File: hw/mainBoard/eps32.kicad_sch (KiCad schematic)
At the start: 13 parts, among them SW1 SW_Push, SW2 SW_Push, U1 ESP32-WROOM-E, U4 TLV76133DCYR

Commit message: finale bez rybicky
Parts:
- U2: renamed from U4; footprint SOT_8DCYR_TEX -> TLV761:SOT_8DCYR_TEX
- renumbered C6 to C1, C7 to C2, C1 to C4, C2 to C5, C5 to C8, C4 to C9
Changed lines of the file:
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@@
   (symbol (lib_id "Device:C") (at 93.98 116.84 90) (unit 1)
     (in_bom yes) (on_board yes) (dnp no)
-    (property "Reference" "C7" (at 93.98 120.65 90)
+    (property "Reference" "C2" (at 93.98 120.65 90)
       (effects (font (size 1.27 1.27)))
     )
@@
       (project "mainBoard"
         (path "/afbe4b5f-4e5c-4a12-a44b-208d158a3f7a/b91751a5-b1b1-4084-8612-1e1796d0f474"
-          (reference "C7") (unit 1)
+          (reference "C2") (unit 1)
         )
       )
@@
   (symbol (lib_id "Device:C") (at 68.58 38.1 0) (unit 1)
     (in_bom yes) (on_board yes) (dnp no) (fields_autoplaced)
-    (property "Reference" "C4" (at 72.39 36.83 0)
+    (property "Reference" "C9" (at 72.39 36.83 0)
       (effects (font (size 1.27 1.27)) (justify left))
     )
@@
       (project "mainBoard"
         (path "/afbe4b5f-4e5c-4a12-a44b-208d158a3f7a/b91751a5-b1b1-4084-8612-1e1796d0f474"
-          (reference "C4") (unit 1)
+          (reference "C9") (unit 1)
         )
       )
@@
   (symbol (lib_id "Device:C") (at 45.72 116.84 90) (unit 1)
     (in_bom yes) (on_board yes) (dnp no)
-    (property "Reference" "C6" (at 45.72 120.65 90)
+    (property "Reference" "C1" (at 45.72 120.65 90)
       (effects (font (size 1.27 1.27)))
     )
@@
       (project "mainBoard"
         (path "/afbe4b5f-4e5c-4a12-a44b-208d158a3f7a/b91751a5-b1b1-4084-8612-1e1796d0f474"
-          (reference "C6") (unit 1)
+          (reference "C1") (unit 1)
         )
       )
@@
   (symbol (lib_id "Device:C") (at 93.98 81.28 0) (unit 1)
     (in_bom yes) (on_board yes) (dnp no) (fields_autoplaced)
-    (property "Reference" "C2" (at 97.79 80.01 0)
+    (property "Reference" "C5" (at 97.79 80.01 0)
       (effects (font (size 1.27 1.27)) (justify left))
     )
@@
       (project "mainBoard"
         (path "/afbe4b5f-4e5c-4a12-a44b-208d158a3f7a/b91751a5-b1b1-4084-8612-1e1796d0f474"
-          (reference "C2") (unit 1)
+          (reference "C5") (unit 1)
         )
       )
@@
   (symbol (lib_id "TLV761:PTLV76118DCYR") (at 54.61 27.94 0) (unit 1)
     (in_bom yes) (on_board yes) (dnp no)
-    (property "Reference" "U4" (at 85.09 20.32 0)
+    (property "Reference" "U2" (at 85.09 20.32 0)
       (effects (font (size 1.524 1.524)))
     )
@@
       (effects (font (size 1.524 1.524)))
     )
-    (property "Footprint" "SOT_8DCYR_TEX" (at 54.61 27.94 0)
+    (property "Footprint" "TLV761:SOT_8DCYR_TEX" (at 54.61 27.94 0)
       (effects (font (size 1.27 1.27) italic) hide)
     )
@@
       (project "mainBoard"
         (path "/afbe4b5f-4e5c-4a12-a44b-208d158a3f7a/b91751a5-b1b1-4084-8612-1e1796d0f474"
-          (reference "U4") (unit 1)
+          (reference "U2") (unit 1)
         )
       )
@@
   (symbol (lib_id "Device:C") (at 111.76 35.56 0) (unit 1)
     (in_bom yes) (on_board yes) (dnp no) (fields_autoplaced)
-    (property "Reference" "C5" (at 115.57 34.29 0)
+    (property "Reference" "C8" (at 115.57 34.29 0)
       (effects (font (size 1.27 1.27)) (justify left))
     )
@@
       (project "mainBoard"
         (path "/afbe4b5f-4e5c-4a12-a44b-208d158a3f7a/b91751a5-b1b1-4084-8612-1e1796d0f474"
-          (reference "C5") (unit 1)
+          (reference "C8") (unit 1)
         )
       )
@@
   (symbol (lib_id "Device:C") (at 45.72 68.58 0) (unit 1)
     (in_bom yes) (on_board yes) (dnp no) (fields_autoplaced)
-    (property "Reference" "C1" (at 49.53 67.31 0)
+    (property "Reference" "C4" (at 49.53 67.31 0)
       (effects (font (size 1.27 1.27)) (justify left))
     )
@@
       (project "mainBoard"
         (path "/afbe4b5f-4e5c-4a12-a44b-208d158a3f7a/b91751a5-b1b1-4084-8612-1e1796d0f474"
-          (reference "C1") (unit 1)
-        )
-      )
+          (reference "C4") (unit 1)
+        )
+      )

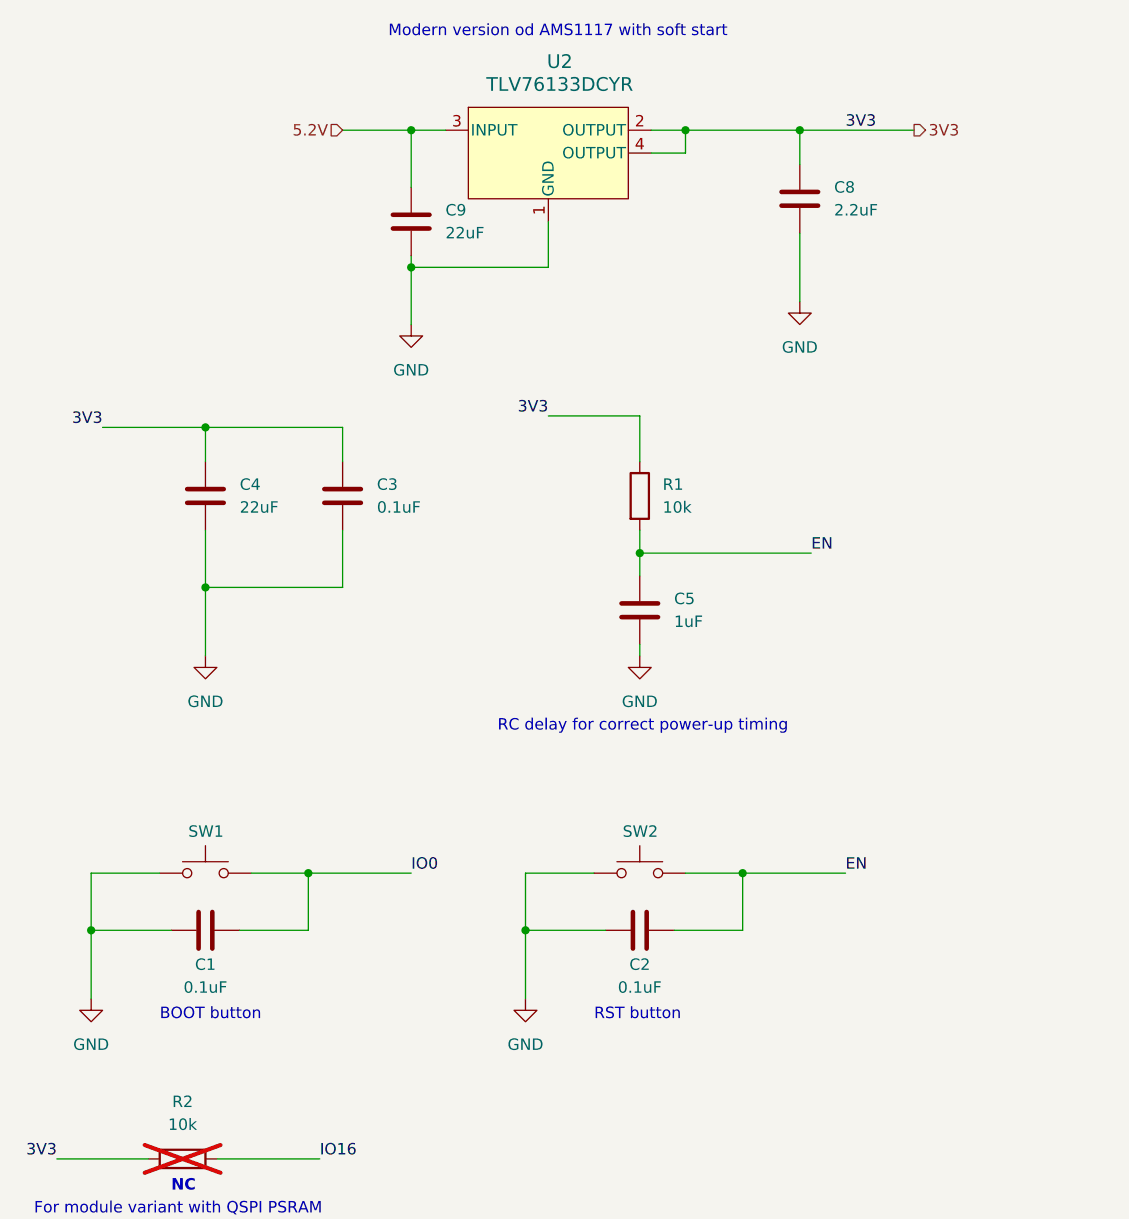
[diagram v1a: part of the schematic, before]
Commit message: text - periferie, obrazky hw - schemata
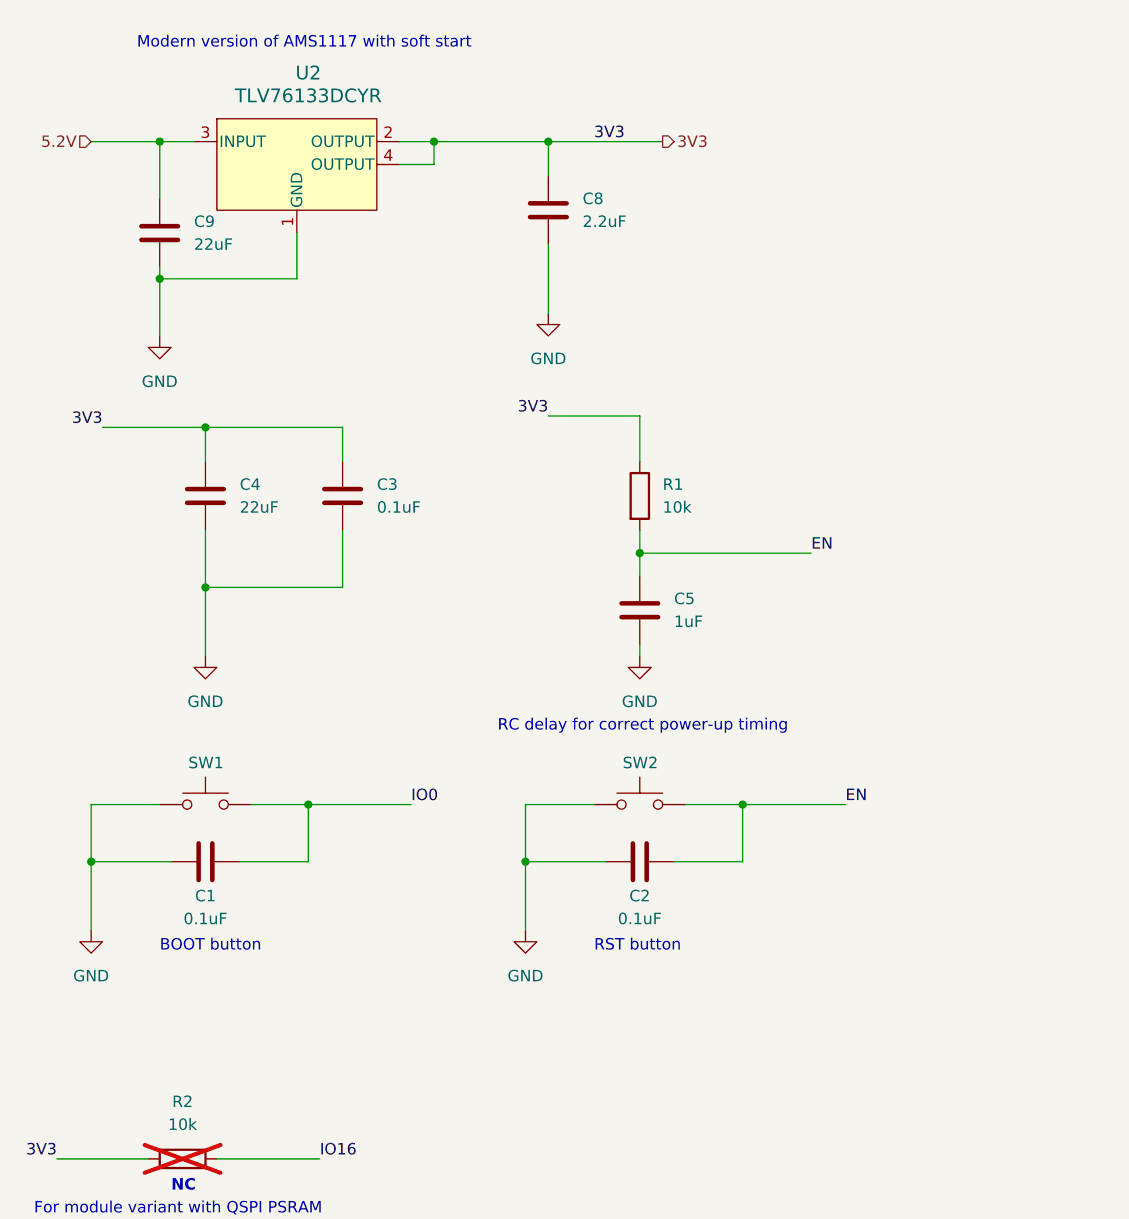
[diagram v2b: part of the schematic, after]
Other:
- note added: "Modern version of AMS1117 with soft start"
- note removed: "Modern version od AMS1117 with soft start"
- moved on the sheet: C1, C2, C8, C9, SW1, SW2, U2
